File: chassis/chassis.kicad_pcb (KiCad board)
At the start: 2 copper layers, 80 parts, among them J1 RJ45_LED_Shielded, Q1 FDG1024NZ, Q2 MMDT3906, U1 S558-5500-25-F, U2 TPS23754PWPR, U3 TCMT1107, U4 L78L33_SO8, U5 KSZ8081RND, U6 EFM32GG11B8xx

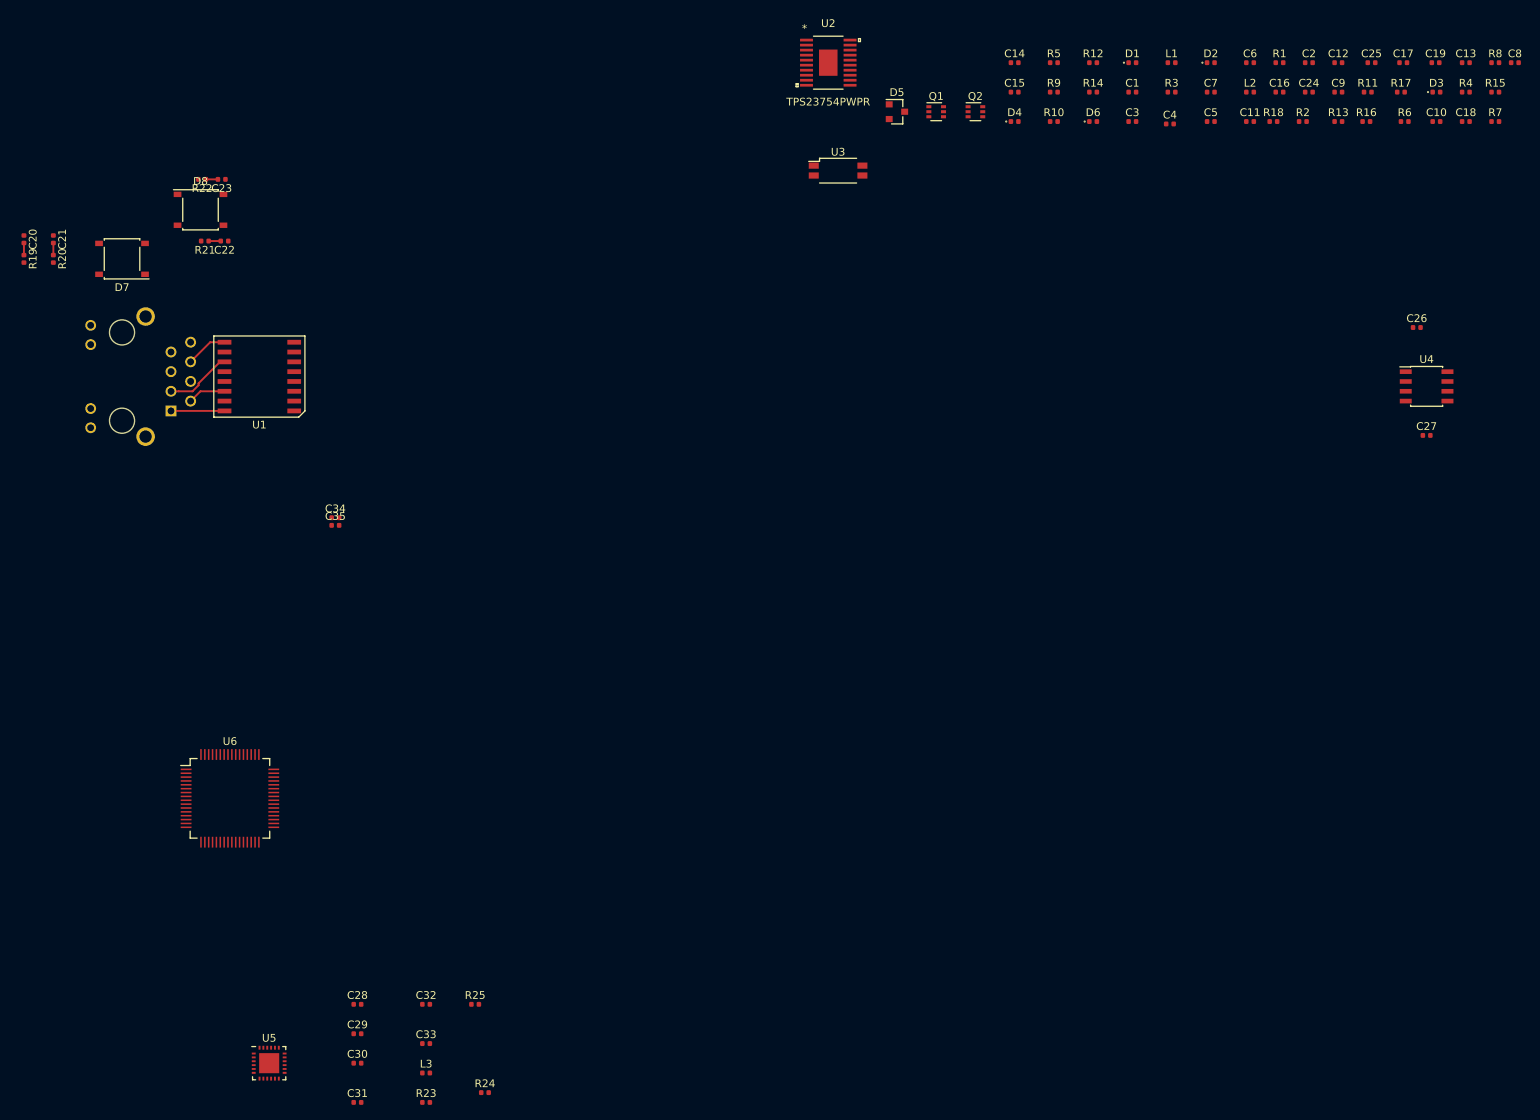
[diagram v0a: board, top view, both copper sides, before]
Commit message: hardware/*: various fixes based on review
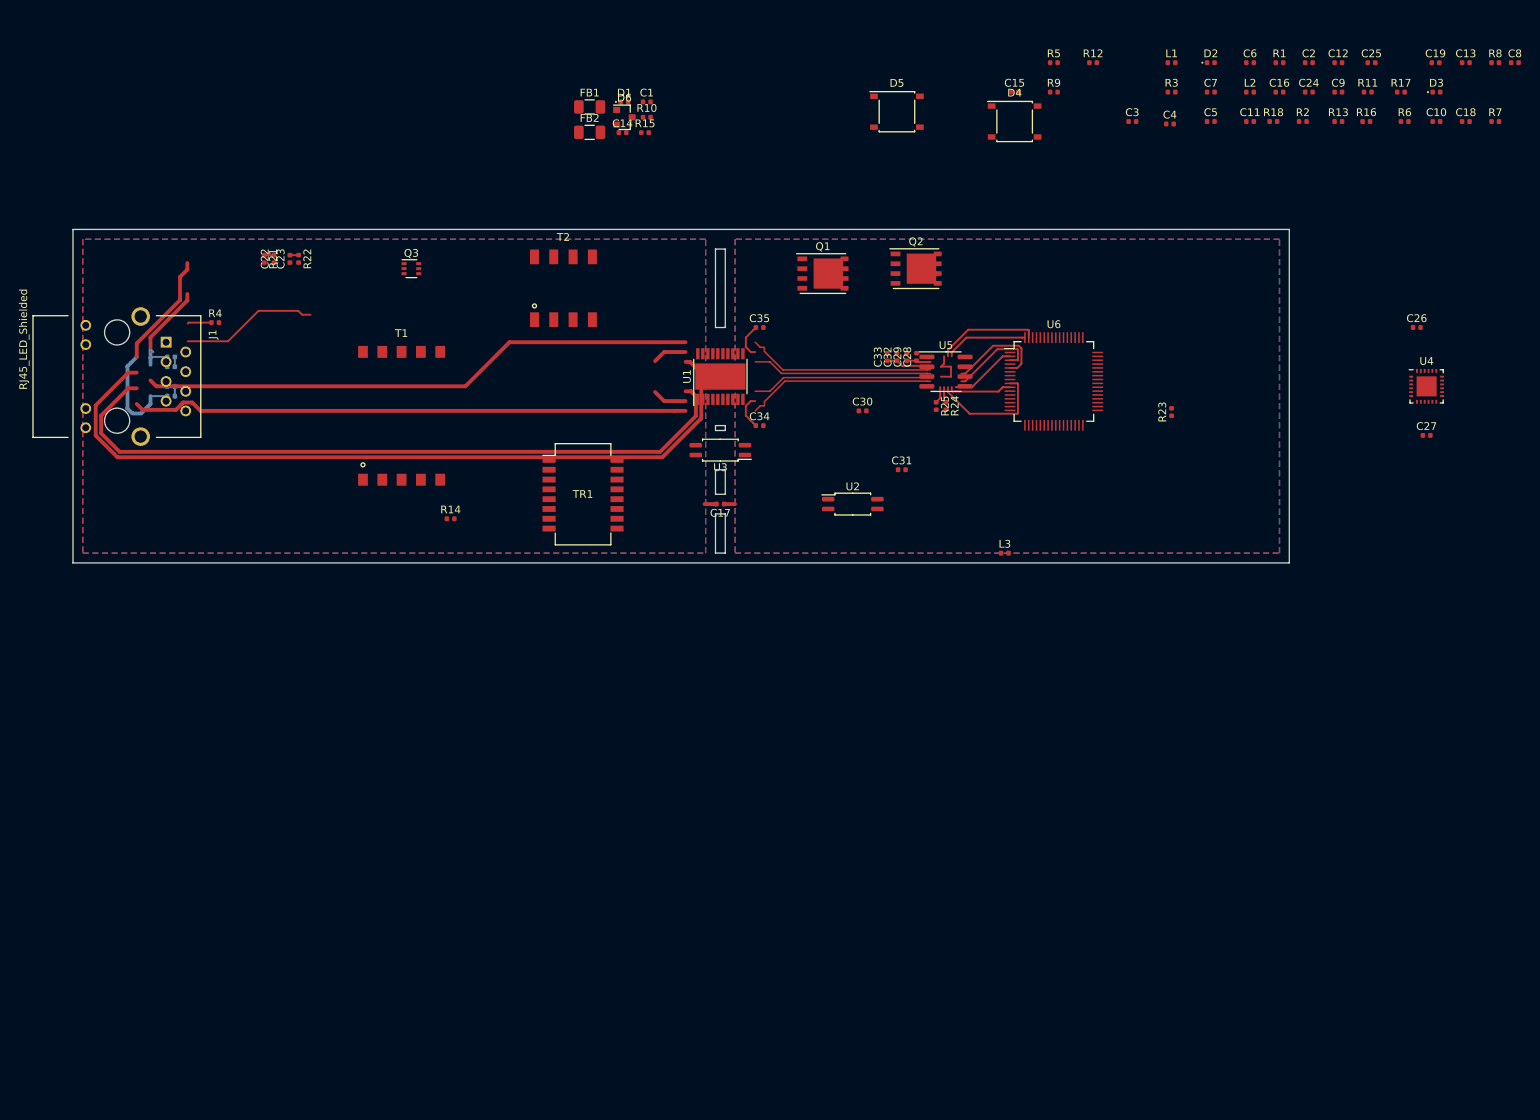
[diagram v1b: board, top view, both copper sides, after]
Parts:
- removed D7, D8: D_Bridge_+-AA, Diode_SMD:Diode_Bridge_Diotec_ABS
- added FB1: Ferrite_Bead_Small, Resistor_SMD:R_1206_3216Metric, F.Cu at (155.8, 47.6)
- added FB2: Ferrite_Bead_Small, Resistor_SMD:R_1206_3216Metric, F.Cu at (155.8, 50.9)
- added Q3: MMDT3906, Package_TO_SOT_SMD:SOT-363_SC-70-6, F.Cu at (132.7, 68.6)
- added T1: PoE_Transformer, chassis:POE_EP13, F.Cu at (131.4, 87.6)
- added T2: Pulse_Transformer, chassis:GDTI_EP7, F.Cu at (152.4, 71.1)
- added TR1: PT61017PEL, Transformer_SMD:Transformer_Ethernet_Bourns_PT61017PEL, F.Cu at (154.9, 97.8)
- C1: value 10n -> 0u1
- C10: value 330u -> 1n2
- C12: value 1u -> 22u
- C13: value 22u -> 1n
- C14: value 1n -> 0u1
- C15: value 0u1 -> 2u2
- C16: value 10n -> 1u
- C17: value 2u2 -> 0u47
- C18: value 1u -> 0u01
- C19: value 0u47 -> 0u01
- C2: value 1u2 -> 47u
- C20, C21: moved to B.Cu
- C22: value 0u01 -> 0u47
- C23: value 0u01 -> 330p
- C24: value 0u47 -> 3n3
- C25: value 3n3 -> 1n
- C26: value 0u33 -> 2u2
- C28: value 2u2 -> 22
- C3: value 0u1 -> 1u
- C32: value 22 -> 0u1
- C34: value 0u1 -> 0u33
- C4: value 47u -> 1u
- C5: value 1u -> 0u1
- C6: value 1u -> 141u
- C7: value 0u1 -> 330u
- C8: value 141u -> 330u
- C9: value 330u -> 1u
- D1: value D_Zener -> D
- D3: value D -> D_Zener
- D4: value D_Zener -> D_Bridge_+-AA; footprint Diode_SMD:D_0402_1005Metric -> Diode_SMD:Diode_Bridge_Diotec_ABS
- D5: value TL431DBZ -> D_Bridge_+-AA; footprint Package_TO_SOT_SMD:SOT-23 -> Diode_SMD:Diode_Bridge_Diotec_ABS
- D6: value D_Zener -> TL431DBZ; footprint Diode_SMD:D_0402_1005Metric -> Package_TO_SOT_SMD:SOT-23
- J1: moved to F.Cu
- L2: value 3u3 -> 0u33
- Q1: value FDG1024NZ -> SiR422DP; footprint Package_TO_SOT_SMD:SOT-363_SC-70-6 -> Package_SO:PowerPAK_SO-8_Single
- Q2: value MMDT3906 -> Si7898DP; footprint Package_TO_SOT_SMD:SOT-363_SC-70-6 -> Package_SO:PowerPAK_SO-8_Single
- R1, R4: value 68 -> 82
- R10: value 69K8 -> 10
- R11: value ? -> 63R4
- R12: value 69K8 -> 0R18
- R13: value 10 -> 10k
- R14: value 63R4 -> 2k
- R15: value 1K -> 75
- R16: value 0R18 -> 75
- R17: value 2K -> 75
- R18: value 10K -> 75
- R19: value 75 -> 1k; moved to B.Cu
- R2: value 10 -> 39K
- R20: value 75 -> 115k; moved to B.Cu
- R21: value 75 -> 560
- R22: value 75 -> 13k3
- R23: value 1K -> 1k
- R24: value 6K49 -> 6k49
- R3: value 39K -> 10
- R5: value 24K9 -> 24k9
- R7: value 130K -> 22k1
- R8: value 15K -> 69k8
- R9: value 38K3 -> 69k8
- U1: value S558-5500-25-F -> TPS23754PWPR; footprint chassis:SOIC-16 -> Package_SO:HTSSOP-20-1EP_4.4x6.5mm_P0.65mm_EP3.4x6.5mm
- U2: value TPS23754PWPR -> TCMT1107; footprint chassis:TSSOP-20 -> Package_SO:SOP-4_4.4x2.6mm_P1.27mm
- U3: footprint Package_SO:SOP-4_4.4x2.8mm_P1.27mm -> Package_SO:SOP-4_4.4x2.6mm_P1.27mm
- U4: value L78L33_SO8 -> KSZ8081RND; footprint Package_SO:SOIC-8_3.9x4.9mm_P1.27mm -> chassis:QFN-24
- U5: value KSZ8081RND -> L78L33_SO8; footprint chassis:QFN-24 -> Package_SO:SOIC-8_3.9x4.9mm_P1.27mm
- moved R4 164.7 mm to (107.3, 75.6)
- moved R23 131.6 mm to (231.1, 87.1), turned to 90 degrees
- moved U5 125.3 mm to (201.9, 81.9)
- moved U6 119.6 mm to (215.9, 83.2)
- moved C29 112.9 mm to (196.8, 80.0), turned to 90 degrees
- moved C28 110.8 mm to (198.1, 80.0), turned to 90 degrees
- moved R15 110.2 mm to (163.0, 51.0)
- moved C31 108.1 mm to (196.2, 94.6)
- moved C33 107.1 mm to (194.3, 80.0), turned to 90 degrees
- moved R24 107.1 mm to (201.9, 86.4), turned to 270 degrees
- moved C30 106.8 mm to (191.1, 87.0)
- moved C17 105.3 mm to (172.7, 99.1), turned to 180 degrees
- moved C32 103.6 mm to (195.6, 80.0), turned to 90 degrees
- moved L3 100.7 mm to (209.6, 105.4)
- moved R14 99.9 mm to (137.8, 101.0)
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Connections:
- C1 pad 2: VDDA -> GNDA
- C10 pad 1: GND -> Net-(C10-Pad1)
- C10 pad 2: +12V -> Net-(C10-Pad2)
- C11 pad 1: GND -> /VC
- C11 pad 2: +12V -> GNDA
- C12 pad 1: Net-(C12-Pad1) -> /VC
- C13 pad 1: Net-(C12-Pad1) -> VDDA
- C13 pad 2: GNDA -> VSSA
- C14 pad 1: VDDA -> Net-(C1-Pad1)
- C14 pad 2: VSSA -> Net-(C14-Pad2)
- C15 pad 1: VDDA -> GNDD
- C15 pad 2: VSSA -> GNDA
- C16 pad 1: Net-(C16-Pad1) -> /VB
- C16 pad 2: Net-(C16-Pad2) -> GNDA
- C17 pad 1: GND -> Net-(C17-Pad1)
- C17 pad 2: GNDA -> Net-(C17-Pad2)
- C18 pad 1: /VB -> Net-(C18-Pad1)
- C18 pad 2: GNDA -> Net-(C18-Pad2)
- C19 pad 2: (no net) -> Net-(C19-Pad2)
- C2 pad 1: Net-(C2-Pad1) -> Net-(C1-Pad1)
- C2 pad 2: Net-(C2-Pad2) -> GNDA
- C23 pad 1: Net-(C23-Pad1) -> GNDA
- C24 pad 1: (no net) -> /VB
- C24 pad 2: Net-(C24-Pad2) -> /CTL
- C25 pad 1: /VB -> Earth
- C25 pad 2: /CTL -> Net-(C25-Pad2)
- C26 pad 1: +12V -> /1V2
- C27 pad 1: +3V3 -> /1V2
- C28 pad 1: /1V2 -> +3V3
- C29 pad 1: /1V2 -> +3V3
- C3 pad 1: Net-(C1-Pad1) -> Net-(C3-Pad1)
- C30 pad 1: +3V3 -> /3V3
- C31 pad 1: +3V3 -> /3V3
- C32 pad 1: /3V3 -> ETH_TX_C
- C33 pad 1: /3V3 -> ETH_RX_C
- C34 pad 1: ETH_TX_C -> +12V
- C34 pad 2: GND -> GNDD
- C35 pad 1: ETH_RX_C -> +3V3
- C35 pad 2: GND -> GNDD
- C4 pad 1: Net-(C1-Pad1) -> Net-(C3-Pad1)
- C5 pad 1: Net-(C5-Pad1) -> Net-(C3-Pad1)
- C5 pad 2: GNDA -> Net-(C5-Pad2)
- C6 pad 1: Net-(C5-Pad1) -> Net-(C6-Pad1)
- C6 pad 2: GNDA -> GNDD
- C7 pad 1: Net-(C5-Pad1) -> Net-(C6-Pad1)
- C7 pad 2: Net-(C7-Pad2) -> GNDD
- C8 pad 1: GND -> +12V
- C8 pad 2: Net-(C8-Pad2) -> GNDD
- C9 pad 1: GND -> +12V
- C9 pad 2: Net-(C8-Pad2) -> GNDD
- D1 pad 1: Net-(C1-Pad1) -> Net-(C5-Pad2)
- D1 pad 2: VDDA -> Net-(D1-Pad2)
- D2 pad 1: Net-(C7-Pad2) -> /VC
- D2 pad 2: (no net) -> Net-(D2-Pad2)
- D3 pad 1: Net-(C12-Pad1) -> Net-(C1-Pad1)
- D3 pad 2: Net-(D3-Pad2) -> Net-(C14-Pad2)
- D5 pad 1: Net-(C16-Pad1) -> VDDA
- D5 pad 2: Net-(C16-Pad2) -> VSSA
- D5 pad 3: GND -> Net-(C20-Pad1)
- D6 pad 1: GNDA -> Net-(D6-Pad1)
- D6 pad 2: VSSA -> Net-(D6-Pad2)
- J1 pad 10: ETH_LED_ACT -> Net-(J1-Pad10)
- J1 pad 11: Net-(J1-Pad11) -> POE_LED
- J1 pad 12: POE_LED -> Net-(J1-Pad12)
- J1 pad 4: Net-(C21-Pad1) -> Net-(C19-Pad1)
- J1 pad 5: Net-(C21-Pad1) -> Net-(C19-Pad1)
- J1 pad 7: Net-(C20-Pad1) -> Net-(C18-Pad1)
- J1 pad 8: Net-(C20-Pad1) -> Net-(C18-Pad1)
- J1 pad 9: Net-(J1-Pad9) -> ETH_LED
- L1 pad 2: Net-(C5-Pad1) -> Net-(C3-Pad1)
- L2 pad 1: Net-(C8-Pad2) -> Net-(C6-Pad1)
- Q1 pad 1: GND -> GNDD
- Q1 pad 2: Net-(Q1-Pad2) -> GNDD
- Q1 pad 3: Net-(C7-Pad2) -> GNDD
- Q1 pad 5: Net-(Q1-Pad5) -> Net-(C10-Pad2)
- Q2 pad 1: GND -> Net-(C23-Pad2)
- Q2 pad 2: Net-(C19-Pad1) -> Net-(C23-Pad2)
- Q2 pad 3: (no net) -> Net-(C23-Pad2)
- Q2 pad 4: (no net) -> Net-(Q2-Pad4)
- Q2 pad 5: (no net) -> Net-(D1-Pad2)
- R1 pad 1: Net-(J1-Pad9) -> Net-(J1-Pad10)
- R10 pad 1: Net-(R10-Pad1) -> Net-(Q2-Pad4)
- R10 pad 2: VDDA -> Net-(R10-Pad2)
- R11 pad 2: Net-(C8-Pad2) -> Net-(C14-Pad2)
- R12 pad 1: Net-(R12-Pad1) -> GNDA
- R12 pad 2: VDDA -> Net-(C23-Pad2)
- R13 pad 1: Net-(Q1-Pad5) -> GNDD
- R13 pad 2: Net-(R13-Pad2) -> Net-(C17-Pad1)
- R14 pad 1: Net-(R14-Pad1) -> /VB
- R14 pad 2: VSSA -> /CTL
- R15 pad 1: Net-(Q1-Pad4) -> Net-(C18-Pad2)
- R15 pad 2: Net-(R15-Pad2) -> Net-(C25-Pad2)
- R16 pad 1: GNDA -> Net-(C19-Pad2)
- R16 pad 2: Net-(Q1-Pad4) -> Net-(C25-Pad2)
- R17 pad 1: /VB -> Net-(C20-Pad2)
- R17 pad 2: /CTL -> Net-(C25-Pad2)
- R18 pad 1: GND -> Net-(C21-Pad2)
- R18 pad 2: Net-(C19-Pad1) -> Net-(C25-Pad2)
- R19 pad 1: Net-(C20-Pad2) -> Net-(D6-Pad1)
- R19 pad 2: Earth -> Net-(R19-Pad2)
- R2 pad 1: GND -> Net-(C3-Pad1)
- R2 pad 2: Net-(C2-Pad1) -> Net-(C5-Pad2)
- R20 pad 1: Net-(C21-Pad2) -> Net-(D6-Pad2)
- R20 pad 2: Earth -> +12V
- R21 pad 1: Net-(C22-Pad2) -> /VC
- R21 pad 2: Earth -> Net-(R21-Pad2)
- R22 pad 1: Net-(C23-Pad2) -> GNDD
- R22 pad 2: Earth -> Net-(D6-Pad2)
- R3 pad 1: Net-(C5-Pad1) -> GNDD
- R3 pad 2: Net-(C7-Pad2) -> Net-(C10-Pad1)
- R4 pad 1: Net-(J1-Pad11) -> Net-(J1-Pad12)
- R5 pad 2: VDDA -> Net-(C1-Pad1)
- R6 pad 1: (no net) -> Net-(D2-Pad2)
- R6 pad 2: Net-(D3-Pad2) -> Net-(R6-Pad2)
- R7 pad 1: Net-(C16-Pad2) -> Net-(R7-Pad1)
- R7 pad 2: Net-(C8-Pad2) -> GNDA
- R8 pad 1: GND -> Net-(R8-Pad1)
- R8 pad 2: Net-(C16-Pad2) -> GNDA
- R9 pad 2: VDDA -> GNDA
- U1 pad 1: ETH_TX_P -> /CTL
- U1 pad 10: Net-(C22-Pad1) -> VSSA
- U1 pad 11: Net-(J1-Pad3) -> Net-(C1-Pad1)
- U1 pad 12: (no net) -> Net-(C1-Pad1)
- U1 pad 13: (no net) -> Net-(R5-Pad1)
- U1 pad 14: Net-(J1-Pad2) -> Net-(C14-Pad2)
- U1 pad 15: Net-(C23-Pad1) -> Net-(R11-Pad1)
- U1 pad 16: Net-(J1-Pad1) -> Net-(R7-Pad1)
- U1 pad 2: ETH_TX_C -> /VB
- U1 pad 3: ETH_TX_M -> Net-(C23-Pad2)
- U1 pad 4: (no net) -> GNDA
- U1 pad 5: (no net) -> Net-(R10-Pad2)
- U1 pad 6: ETH_RX_P -> /VC
- U1 pad 7: ETH_RX_C -> Net-(C22-Pad2)
- U1 pad 8: ETH_RX_M -> GNDA
- U1 pad 9: Net-(J1-Pad6) -> GNDA
- U2 pad 1: /CTL -> +12V
- U2 pad 2: /VB -> Net-(R19-Pad2)
- U2 pad 3: Net-(R15-Pad2) -> GNDA
- U2 pad 4: GNDA -> /CTL
- U3 pad 1: Net-(R11-Pad1) -> POE_LED
- U3 pad 2: Net-(C16-Pad1) -> GNDD
- U3 pad 3: GNDA -> /T2P
- U3 pad 4: /CTL -> Net-(R21-Pad2)
- U4 pad 1: +3V3 -> /1V2
- U4 pad 2: GND -> /3V3
- U4 pad 3: GND -> ETH_RX_M
- U4 pad 4: (no net) -> ETH_RX_P
- U4 pad 5: (no net) -> ETH_TX_M
- U4 pad 6: GND -> ETH_TX_P
- U4 pad 7: GND -> Net-(U4-Pad7)
- U4 pad 8: +12V -> Net-(R25-Pad1)
- U5 pad 1: /1V2 -> +3V3
- U5 pad 2: /3V3 -> GNDD
- U5 pad 3: ETH_RX_M -> GNDD
- U5 pad 4: ETH_RX_P -> Net-(U5-Pad4)
- U5 pad 5: ETH_TX_M -> Net-(U5-Pad5)
- U5 pad 6: ETH_TX_P -> GNDD
- U5 pad 7: (no net) -> GNDD
- U5 pad 8: Net-(R25-Pad1) -> +12V
- U6 pad 11: (no net) -> Net-(U6-Pad11)
- U6 pad 12: (no net) -> Net-(U6-Pad12)
- U6 pad 13: (no net) -> Net-(U6-Pad13)
- U6 pad 14: (no net) -> Net-(U6-Pad14)
- U6 pad 15: (no net) -> Net-(U6-Pad15)
- U6 pad 16: (no net) -> Net-(U6-Pad16)
- U6 pad 17: (no net) -> Net-(U6-Pad17)
- U6 pad 18: (no net) -> Net-(U6-Pad18)
- U6 pad 19: (no net) -> Net-(U6-Pad19)
- U6 pad 20: (no net) -> Net-(U6-Pad20)
- U6 pad 21: (no net) -> Net-(U6-Pad21)
- U6 pad 22: (no net) -> Net-(U6-Pad22)
- U6 pad 25: (no net) -> Net-(U6-Pad25)
- U6 pad 26: (no net) -> Net-(U6-Pad26)
- U6 pad 28: (no net) -> Net-(U6-Pad28)
- U6 pad 29: (no net) -> Net-(U6-Pad29)
- U6 pad 30: (no net) -> Net-(U6-Pad30)
- U6 pad 31: (no net) -> Net-(U6-Pad31)
- U6 pad 32: (no net) -> Net-(U6-Pad32)
- U6 pad 33: (no net) -> Net-(U6-Pad33)
- U6 pad 34: (no net) -> Net-(U6-Pad34)
- U6 pad 35: (no net) -> Net-(U6-Pad35)
- U6 pad 36: (no net) -> Net-(U6-Pad36)
- U6 pad 37: (no net) -> Net-(U6-Pad37)
- U6 pad 38: (no net) -> Net-(U6-Pad38)
- U6 pad 40: (no net) -> Net-(U6-Pad40)
- U6 pad 41: (no net) -> Net-(U6-Pad41)
- U6 pad 42: (no net) -> Net-(U6-Pad42)
- U6 pad 43: (no net) -> Net-(U6-Pad43)
- U6 pad 44: (no net) -> Net-(U6-Pad44)
- U6 pad 45: (no net) -> Net-(U6-Pad45)
- U6 pad 46: (no net) -> Net-(U6-Pad46)
- U6 pad 47: (no net) -> Net-(U6-Pad47)
- U6 pad 48: (no net) -> Net-(U6-Pad48)
- U6 pad 51: (no net) -> Net-(U6-Pad51)
- U6 pad 52: (no net) -> Net-(U6-Pad52)
- U6 pad 53: (no net) -> Net-(U6-Pad53)
- U6 pad 54: (no net) -> Net-(U6-Pad54)
- U6 pad 57: (no net) -> Net-(U6-Pad57)
- U6 pad 58: (no net) -> Net-(U6-Pad58)
- U6 pad 59: (no net) -> Net-(U6-Pad59)
- U6 pad 60: (no net) -> Net-(U6-Pad60)
- U6 pad 61: (no net) -> Net-(U6-Pad61)
- U6 pad 62: (no net) -> Net-(U6-Pad62)
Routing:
- net Net-(J1-Pad3): track 8.66 -> 101.1 mm
- net /CTL: track 0.00 -> 92.5 mm
- net Net-(J1-Pad6): track 5.44 -> 72.0 mm
- net Net-(J1-Pad1): track 6.93 -> 72.2 mm
- net Net-(C20-Pad1): track 0.00 -> 29.0 mm
- net ETH_TX_P: track 0.00 -> 24.6 mm
- net ETH_RX_M: track 0.00 -> 24.5 mm
- net GNDD: track 0.00 -> 23.4 mm
- net ETH_RX_P: track 0.00 -> 23.3 mm
- net POE_LED: track 0.00 -> 17.7 mm
- net ETH_MDIO: track 0.00 -> 15.7 mm
- net Net-(C21-Pad1): track 0.00 -> 13.7 mm
- net ETH_RMII_TXD1: track 0.00 -> 13.3 mm
- net ETH_RMII_CRS_DV: track 0.00 -> 13.1 mm
- net ETH_RMII_RXD0: track 0.00 -> 11.4 mm
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- added copper zone on B.Cu, net GND
- added copper zone on F.Cu, net GND
- added copper zone on B.Cu, net GNDA
- added copper zone on F.Cu, net GNDA
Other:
- board outline added: 157.5 x 43.2 mm
- net class Power added: clearance 0.4, trace_width 0.5, via_dia 0.8, via_drill 0.4

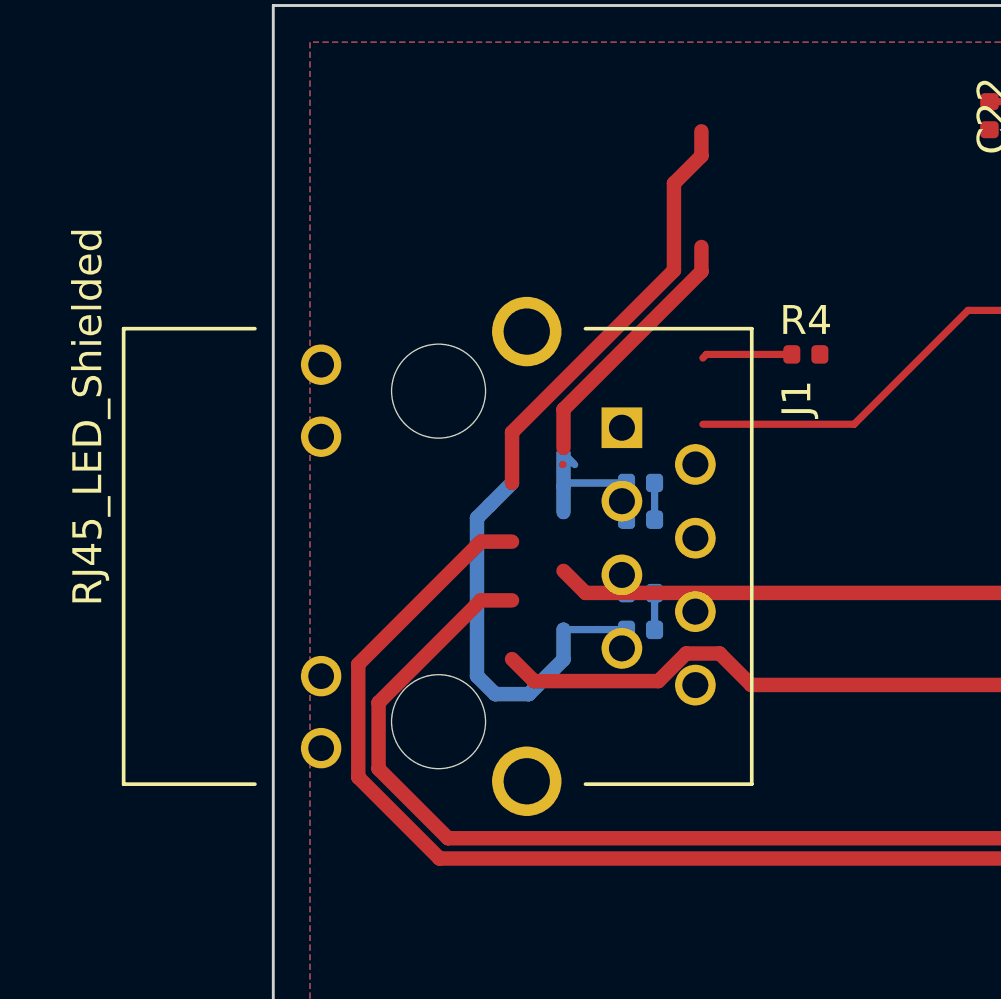
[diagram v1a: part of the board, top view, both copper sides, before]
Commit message: hardware/lib: use new RJ-45 jack
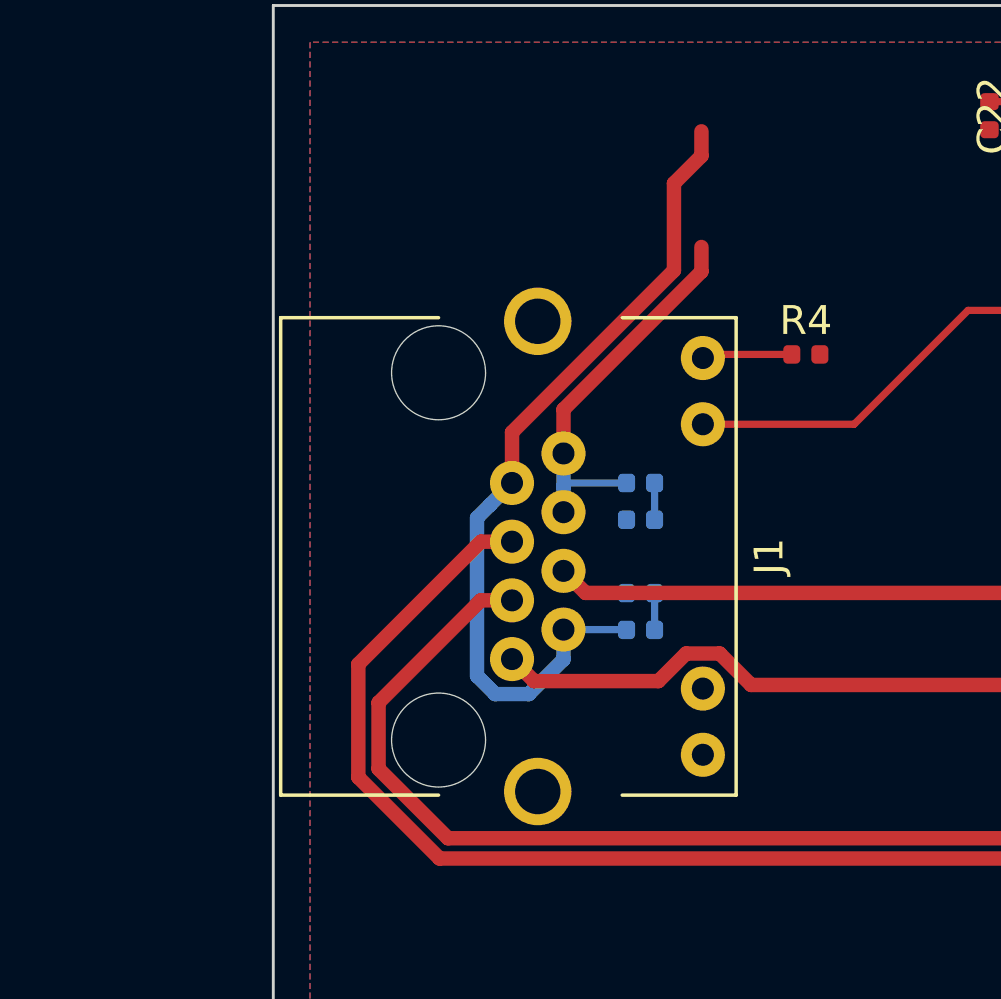
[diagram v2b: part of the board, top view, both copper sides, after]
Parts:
- J1: footprint chassis:RJMG1BD3B8K1ANR -> chassis:RJHSE-538X
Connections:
- C26 pad 2: GND -> GNDD
- C27 pad 2: GND -> GNDD
- C28 pad 2: GND -> GNDD
- C29 pad 2: GND -> GNDD
- C30 pad 2: GND -> GNDD
- C31 pad 2: GND -> GNDD
- C32 pad 2: GND -> GNDD
- C33 pad 2: GND -> GNDD
- R24 pad 2: GND -> GNDD
- U1 pad 20: Net-(U1-Pad20) -> /T2P
- U4 pad 22: GND -> GNDD
- U4 pad 25: GND -> GNDD
- U6 pad 23: GND -> GNDD
- U6 pad 56: GND -> GNDD
- U6 pad 8: GND -> GNDD
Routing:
- added copper zone on F.Cu, net GNDD
- removed copper zone on F.Cu, net GND
